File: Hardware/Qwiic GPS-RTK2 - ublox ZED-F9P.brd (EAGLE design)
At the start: 43.2 x 43.2 mm, 125 parts, among them J1 Radio, J13 U.FL, J3 PTH, U2 3.3V, U3 ZED-F9P

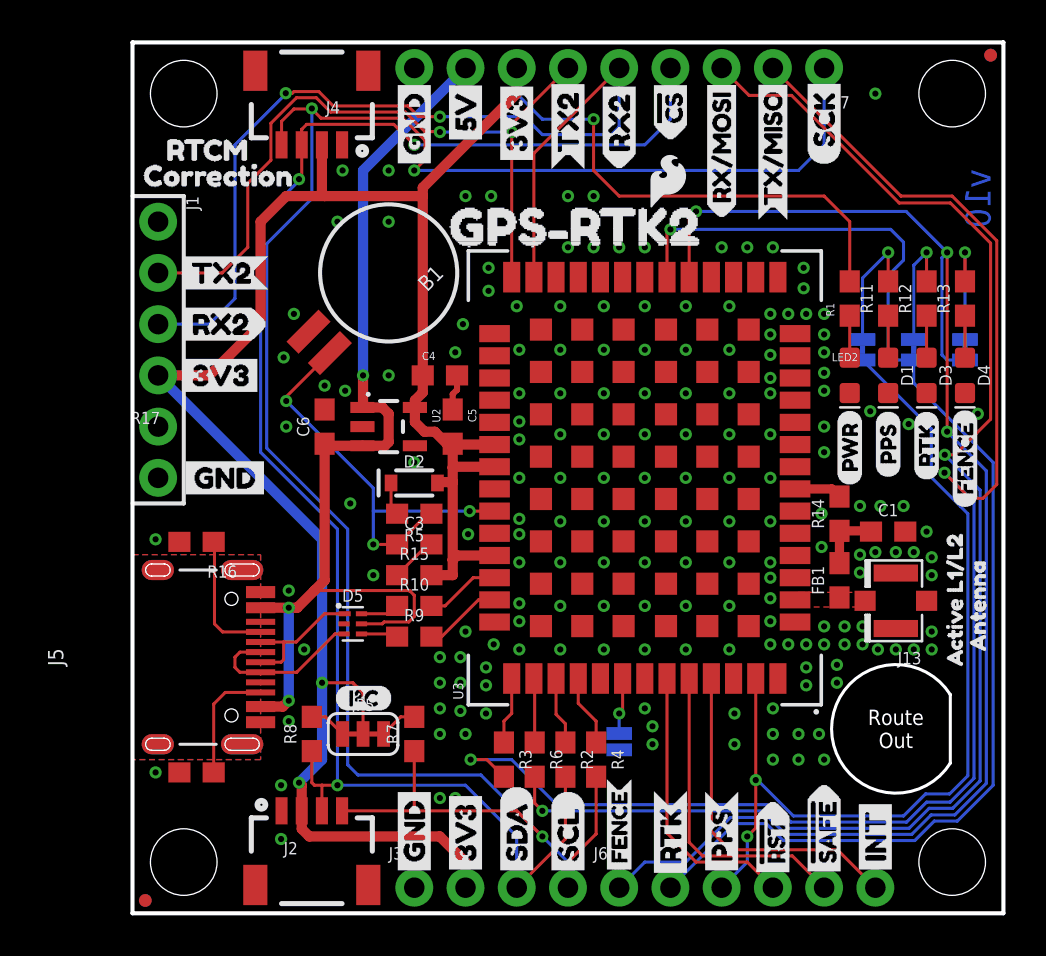
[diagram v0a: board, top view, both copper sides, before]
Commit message: v11 hardware: Added add' decoupling to USB VBUS, recomended induc to ant, more 33 ohm resistors.
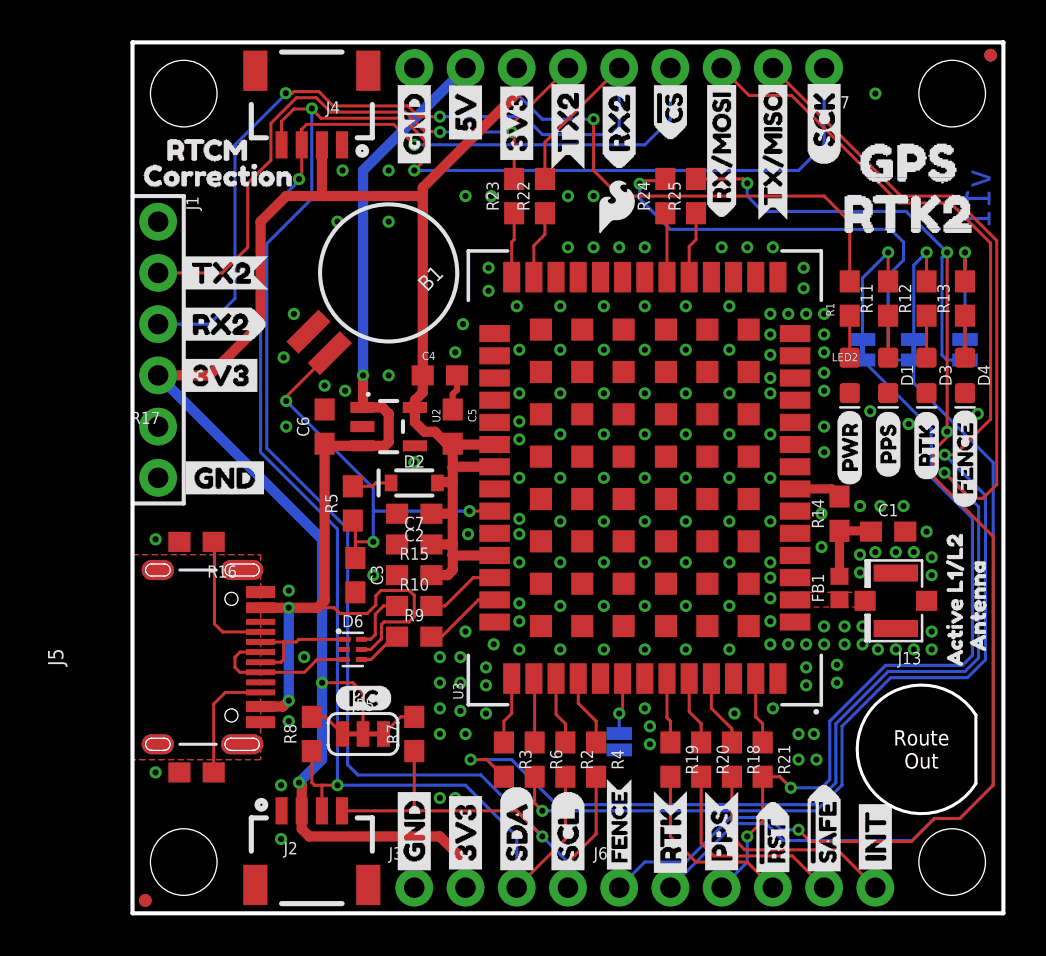
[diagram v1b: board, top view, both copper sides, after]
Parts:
- removed D5: PRTR5V0U2F, funbit:SOT886
- removed U$47: (no value), buzzard_labels (4):GPS#RTK29
- added C2: 1.0uF, SparkFun-Capacitors:0603
- added C7: 0.1uF, SparkFun-Capacitors:0603
- added D6: PRTR5V0U2F, SparkFun-IC-Power:SOT886
- added R18, R19, R20, R21, R22, R23, R24, R25: 33, SparkFun-Resistors:0603
- added U$59: (no value), buzzard_labels (4):GPS0
- added U$64: (no value), buzzard_labels (4):RTK21
- FB1: value 30Ω/1.8A -> FERRITE_BEAD-120_OHM-0402; device SparkFun-Coils:0603 -> SparkFun-Coils:0402
- J5: device USB-C:USB-C-16P -> SparkFun-Connectors:USB-C-16P
- moved U$2 12.8 mm to (57.1, 54.6)
- moved C3 3.29 mm to (11.0, 16.8), turned to 270 degrees
- moved R5 3.09 mm to (10.9, 20.3), turned to 90 degrees
- moved U$33 2.84 mm to (24.0, 35.1)
- moved U$54 1.63 mm to (39.1, 8.13)
- moved FB1 0.38 mm to (35.1, 16.1)
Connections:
- new net N$14: R22.1, U3.26
- new net N$15: R18.1, U3.51
- new net N$16: R19.1, U3.49
- new net N$17: R21.1, U3.53
- new net N$18: R20.1, U3.50
- new net N$19: R24.1, U3.20
- new net N$20: R25.1, U3.19
- new net TX2_P: R23.1, U3.27
- net !RESET: now also R19.2; no longer U3.49
- net !SAFE: now also R20.2; no longer U3.50
- net 3.3V: now also C2.1, C7.2
- net 5V: now also D6.5; no longer D5.5
- net D+: now also D6.4; no longer D5.4
- net D-: now also D6.6; no longer D5.6
- net FENCE_STAT: now also R25.2; no longer U3.19
- net GND: now also C2.2, C7.1, D6.2; no longer D5.2
- net INT: now also R18.2; no longer U3.51
- net PPS: now also R21.2; no longer U3.53
- net RTK_STAT: now also R24.2; no longer U3.20
- net RX2: now also R22.2; no longer U3.26
- net TX2: now also R23.2; no longer U3.27
- net UNP_D+: now also D6.3; no longer D5.3
- net UNP_D-: now also D6.1; no longer D5.1
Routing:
- net PPS: track 45.9 -> 38.3 mm
- net INT: track 16.9 -> 11.1 mm
- net !SAFE: track 15.7 -> 10.3 mm
- net RX2: track 48.2 -> 43.1 mm
- net !RESET: track 14.0 -> 9.09 mm
- net TX2: track 36.3 -> 31.5 mm
- net N$15: track 0.00 -> 3.59 mm
- net N$18: track 0.00 -> 3.42 mm
- net N$14: track 0.00 -> 3.40 mm
- net N$17: track 0.00 -> 3.31 mm
- net N$20: track 0.00 -> 3.31 mm
- net N$16: track 0.00 -> 3.24 mm
- net TX2_P: track 0.00 -> 3.22 mm
- net N$19: track 0.00 -> 3.20 mm
- net GND: track 4.11 -> 1.78 mm, vias 178 -> 174
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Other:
- board text added: "v11"
- board text removed: "v10"
